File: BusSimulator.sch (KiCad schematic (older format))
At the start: 100 parts, among them IC1 CS30CL, IC2 CS30CL, IC3 CS30CL, J1 CONN_3-6318491-6, J2 OSTTA024163, J3 Conn_01x03, J4 Conn_01x03, J5 Conn_01x02, J6 Conn_01x03, Q1 MOSFET_N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

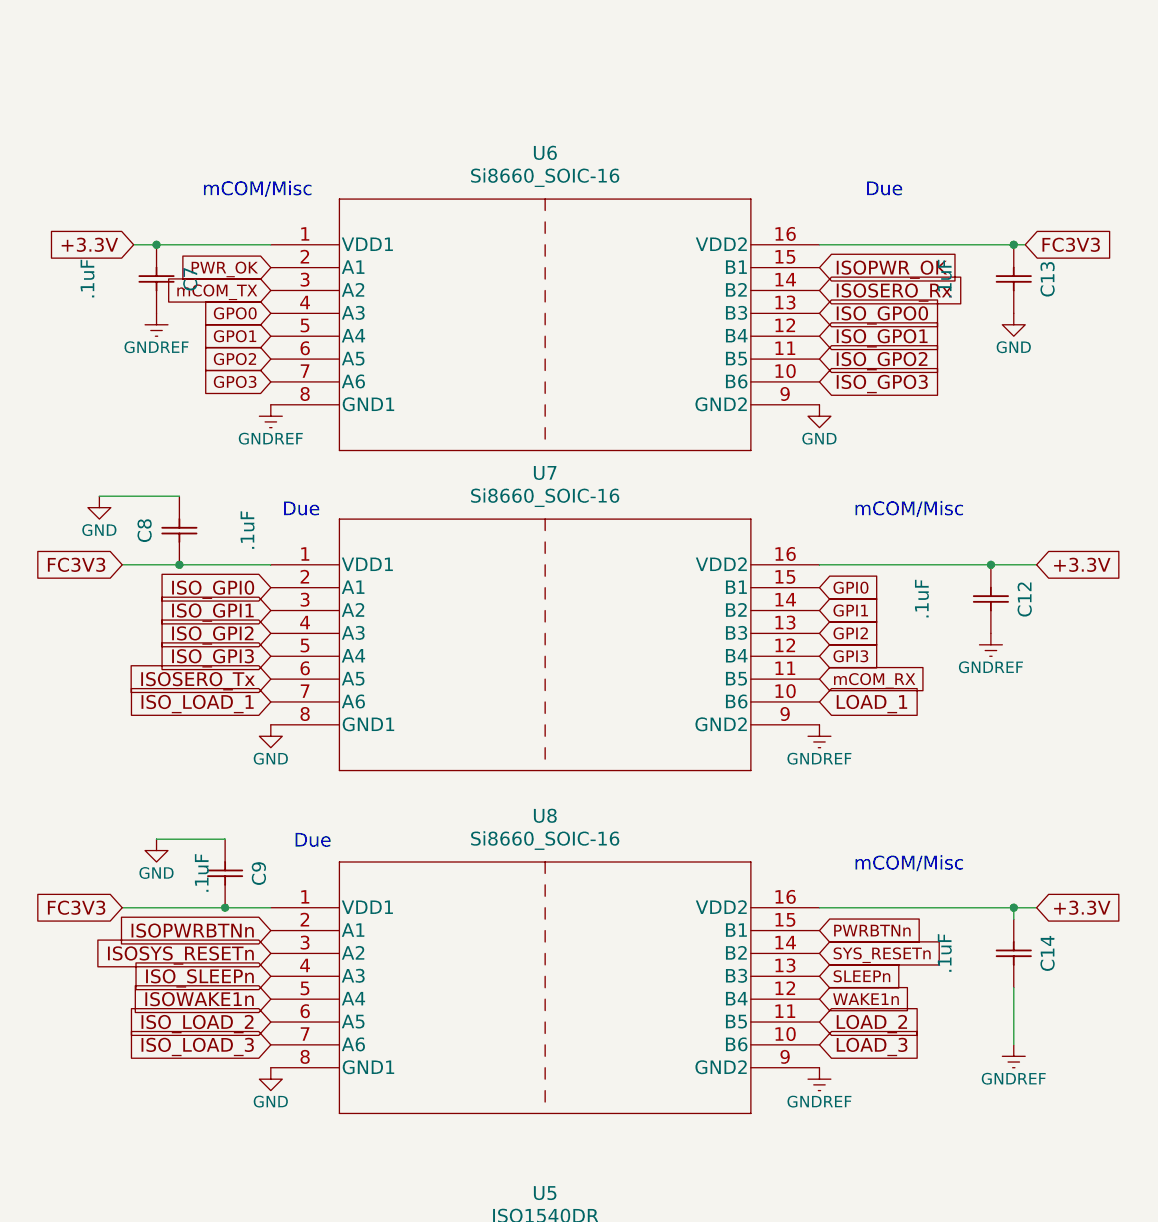
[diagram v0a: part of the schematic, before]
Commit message: Organize isolator nets and arrange PCB components
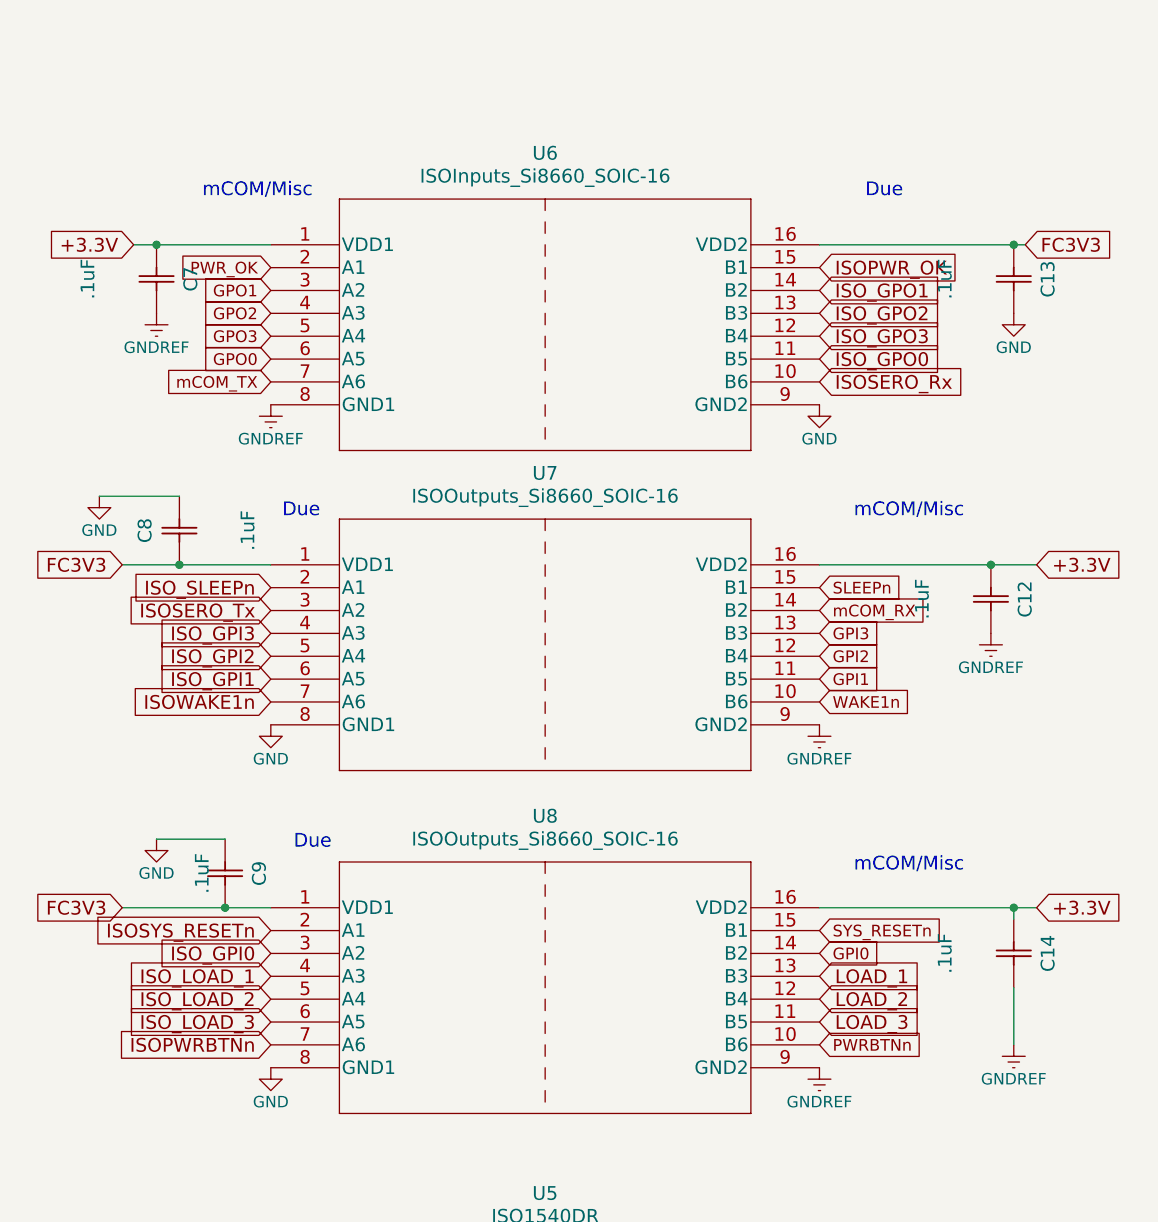
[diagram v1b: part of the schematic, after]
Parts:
- U6: value Si8660_SOIC-16 -> ISOInputs_Si8660_SOIC-16
- U7, U8: value Si8660_SOIC-16 -> ISOOutputs_Si8660_SOIC-16
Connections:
- net GPI0: now also U8.14 (B2); no longer U7.15 (B1)
- net GPI1: now also U7.11 (B5); no longer U7.14 (B2)
- net GPI2: now also U7.12 (B4); no longer U7.13 (B3)
- net GPI3: now also U7.13 (B3); no longer U7.12 (B4)
- net GPO0: now also U6.6 (A5); no longer U6.4 (A3)
- net GPO1: now also U6.3 (A2); no longer U6.5 (A4)
- net GPO2: now also U6.4 (A3); no longer U6.6 (A5)
- net GPO3: now also U6.5 (A4); no longer U6.7 (A6)
- net ISOPWRBTNn: now also U8.7 (A6); no longer U8.2 (A1)
- net ISOSERO_Rx: now also U6.10 (B6); no longer U6.14 (B2)
- net ISOSERO_Tx: now also U7.3 (A2); no longer U7.6 (A5)
- net ISOSYS_RESETn: now also U8.2 (A1); no longer U8.3 (A2)
- net ISOWAKE1n: now also U7.7 (A6); no longer U8.5 (A4)
- net ISO_GPI0: now also U8.3 (A2); no longer U7.2 (A1)
- net ISO_GPI1: now also U7.6 (A5); no longer U7.3 (A2)
- net ISO_GPI2: now also U7.5 (A4); no longer U7.4 (A3)
- net ISO_GPI3: now also U7.4 (A3); no longer U7.5 (A4)
- net ISO_GPO0: now also U6.11 (B5); no longer U6.13 (B3)
- net ISO_GPO1: now also U6.14 (B2); no longer U6.12 (B4)
- net ISO_GPO2: now also U6.13 (B3); no longer U6.11 (B5)
- net ISO_GPO3: now also U6.12 (B4); no longer U6.10 (B6)
- net ISO_LOAD_1: now also U8.4 (A3); no longer U7.7 (A6)
- net ISO_LOAD_2: now also U8.5 (A4); no longer U8.6 (A5)
- net ISO_LOAD_3: now also U8.6 (A5); no longer U8.7 (A6)
- net ISO_SLEEPn: now also U7.2 (A1); no longer U8.4 (A3)
- net LOAD_1: now also U8.13 (B3); no longer U7.10 (B6)
- net LOAD_2: now also U8.12 (B4); no longer U8.11 (B5)
- net LOAD_3: now also U8.11 (B5); no longer U8.10 (B6)
- net PWRBTNn: now also U8.10 (B6); no longer U8.15 (B1)
- net SLEEPn: now also U7.15 (B1); no longer U8.13 (B3)
- net SYS_RESETn: now also U8.15 (B1); no longer U8.14 (B2)
- net WAKE1n: now also U7.10 (B6); no longer U8.12 (B4)
- net mCOM_RX: now also U7.14 (B2); no longer U7.11 (B5)
- net mCOM_TX: now also U6.7 (A6); no longer U6.3 (A2)
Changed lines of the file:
@@
 P 1450 9850
 F 0 "U6" H 2650 10250 60  0000 C CNN
-F 1 "Si8660_SOIC-16" H 2650 10150 60  0000 C CNN
+F 1 "ISOInputs_Si8660_SOIC-16" H 2650 10150 60  0000 C CNN
 F 2 "BusSimulator:SI8660BA-B-IS1" H 2650 10090 60  0001 C CNN
 F 3 "" H 1450 9850 60  0000 C CNN
@@
 	1    0    0    -1
 $EndComp
-Text GLabel 3850 13150 2    51   Input ~ 0
+Text GLabel 3850 11850 2    51   Input ~ 0
 WAKE1n
 Text GLabel 1450 9950 0    51   Input ~ 0
 PWR_OK
-Text GLabel 3850 12950 2    51   Input ~ 0
+Text GLabel 3850 12850 2    51   Input ~ 0
 SYS_RESETn
-Text GLabel 3850 12850 2    51   Input ~ 0
+Text GLabel 3850 13350 2    51   Input ~ 0
 PWRBTNn
 Text GLabel 850  9850 0    60   Input ~ 0
@@
 	1    0    0    -1
 $EndComp
-Text GLabel 1450 13150 0    60   Input ~ 0
+Text GLabel 1450 11850 0    60   Input ~ 0
 ISOWAKE1n
 Text GLabel 3850 9950 2    60   Input ~ 0
 ISOPWR_OK
-Text GLabel 1450 12950 0    60   Input ~ 0
+Text GLabel 1450 12850 0    60   Input ~ 0
 ISOSYS_RESETn
-Text GLabel 1450 12850 0    60   Input ~ 0
+Text GLabel 1450 13350 0    60   Input ~ 0
 ISOPWRBTNn
-Text GLabel 3850 11350 2    51   Input ~ 0
+Text GLabel 3850 12950 2    51   Input ~ 0
 GPI0
-Text GLabel 3850 11450 2    51   Input ~ 0
+Text GLabel 3850 11750 2    51   Input ~ 0
 GPI1
+Text GLabel 3850 11650 2    51   Input ~ 0
+GPI2
 Text GLabel 3850 11550 2    51   Input ~ 0
-GPI2
-Text GLabel 3850 11650 2    51   Input ~ 0
 GPI3
+Text GLabel 1450 10050 0    51   Input ~ 0
+GPO1
+Text GLabel 1450 10150 0    51   Input ~ 0
+GPO2
 Text GLabel 1450 10250 0    51   Input ~ 0
-GPO1
+GPO3
 Text GLabel 1450 10350 0    51   Input ~ 0
-GPO2
-Text GLabel 1450 10450 0    51   Input ~ 0
-GPO3
-Text GLabel 1450 10150 0    51   Input ~ 0
 GPO0
 $Comp
@@
 P 1450 11250
 F 0 "U7" H 2650 11650 60  0000 C CNN
-F 1 "Si8660_SOIC-16" H 2650 11550 60  0000 C CNN
+F 1 "ISOOutputs_Si8660_SOIC-16" H 2650 11550 60  0000 C CNN
 F 2 "BusSimulator:SI8660BA-B-IS1" H 2650 11490 60  0001 C CNN
 F 3 "" H 1450 11250 60  0000 C CNN
@@
 P 1450 12750
 F 0 "U8" H 2650 13150 60  0000 C CNN
-F 1 "Si8660_SOIC-16" H 2650 13050 60  0000 C CNN
+F 1 "ISOOutputs_Si8660_SOIC-16" H 2650 13050 60  0000 C CNN
 F 2 "BusSimulator:SI8660BA-B-IS1" H 2650 12990 60  0001 C CNN
 F 3 "" H 1450 12750 60  0000 C CNN
@@
 	1    0    0    -1
 $EndComp
-Text GLabel 3850 11850 2    60   Input ~ 0
+Text GLabel 3850 13050 2    60   Input ~ 0
 LOAD_1
+Text GLabel 3850 13150 2    60   Input ~ 0
+LOAD_2
 Text GLabel 3850 13250 2    60   Input ~ 0
-LOAD_2
-Text GLabel 3850 13350 2    60   Input ~ 0
 LOAD_3
-Text GLabel 3850 13050 2    51   Input ~ 0
+Text GLabel 3850 11350 2    51   Input ~ 0
 SLEEPn
-Text GLabel 1450 13050 0    60   Input ~ 0
+Text GLabel 1450 11350 0    60   Input ~ 0
 ISO_SLEEPn
 $Comp
@@
 Text GLabel 16400 6900 0    60   Input ~ 0
 DUE_SCL
-Text GLabel 1450 11350 0    60   Input ~ 0
+Text GLabel 1450 12950 0    60   Input ~ 0
 ISO_GPI0
-Text GLabel 1450 11450 0    60   Input ~ 0
+Text GLabel 1450 11750 0    60   Input ~ 0
 ISO_GPI1
+Text GLabel 1450 11650 0    60   Input ~ 0
+ISO_GPI2
 Text GLabel 1450 11550 0    60   Input ~ 0
-ISO_GPI2
-Text GLabel 1450 11650 0    60   Input ~ 0
 ISO_GPI3
+Text GLabel 3850 10350 2    60   Input ~ 0
+ISO_GPO0
+Text GLabel 3850 10050 2    60   Input ~ 0
+ISO_GPO1
 Text GLabel 3850 10150 2    60   Input ~ 0
-ISO_GPO0
+ISO_GPO2
 Text GLabel 3850 10250 2    60   Input ~ 0
-ISO_GPO1
-Text GLabel 3850 10350 2    60   Input ~ 0
-ISO_GPO2
-Text GLabel 3850 10450 2    60   Input ~ 0
 ISO_GPO3
-Text GLabel 1450 11850 0    60   Input ~ 0
+Text GLabel 1450 13050 0    60   Input ~ 0
 ISO_LOAD_1
+Text GLabel 1450 13150 0    60   Input ~ 0
+ISO_LOAD_2
 Text GLabel 1450 13250 0    60   Input ~ 0
-ISO_LOAD_2
-Text GLabel 1450 13350 0    60   Input ~ 0
 ISO_LOAD_3
 Text Notes 6300 950  0    60   ~ 0
@@
 	1    0    0    -1
 $EndComp
-Text GLabel 3850 10050 2    60   Input ~ 0
+Text GLabel 3850 10450 2    60   Input ~ 0
 ISOSERO_Rx
-Text GLabel 1450 11750 0    60   Input ~ 0
+Text GLabel 1450 11450 0    60   Input ~ 0
 ISOSERO_Tx
 Text GLabel 16400 5800 0    60   Input ~ 0
@@
 Text Notes 4000 12600 0    60   ~ 0
 mCOM/Misc
-Text GLabel 1450 10050 0    51   Input ~ 0
+Text GLabel 1450 10450 0    51   Input ~ 0
 mCOM_TX
-Text GLabel 3850 11750 2    51   Input ~ 0
+Text GLabel 3850 11450 2    51   Input ~ 0
 mCOM_RX
 Text Notes 1150 9650 0    60   ~ 0

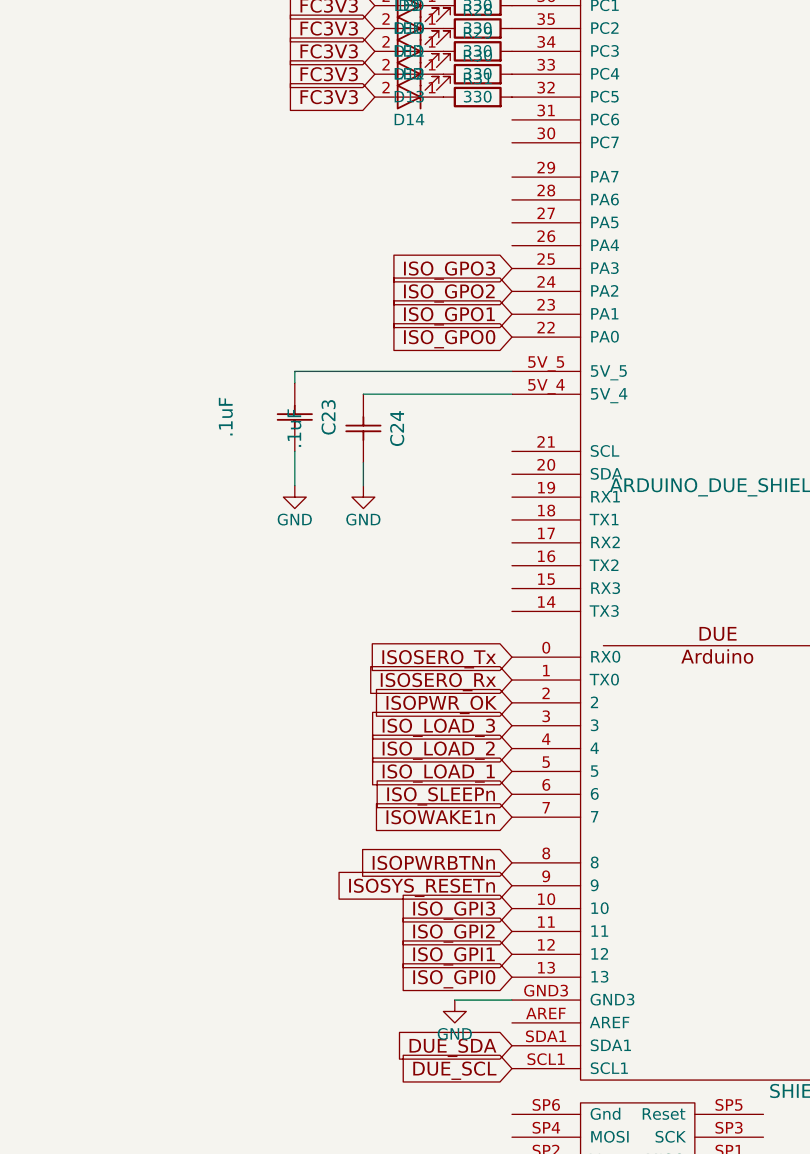
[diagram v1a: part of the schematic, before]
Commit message: Organize Due-to-isolator connection
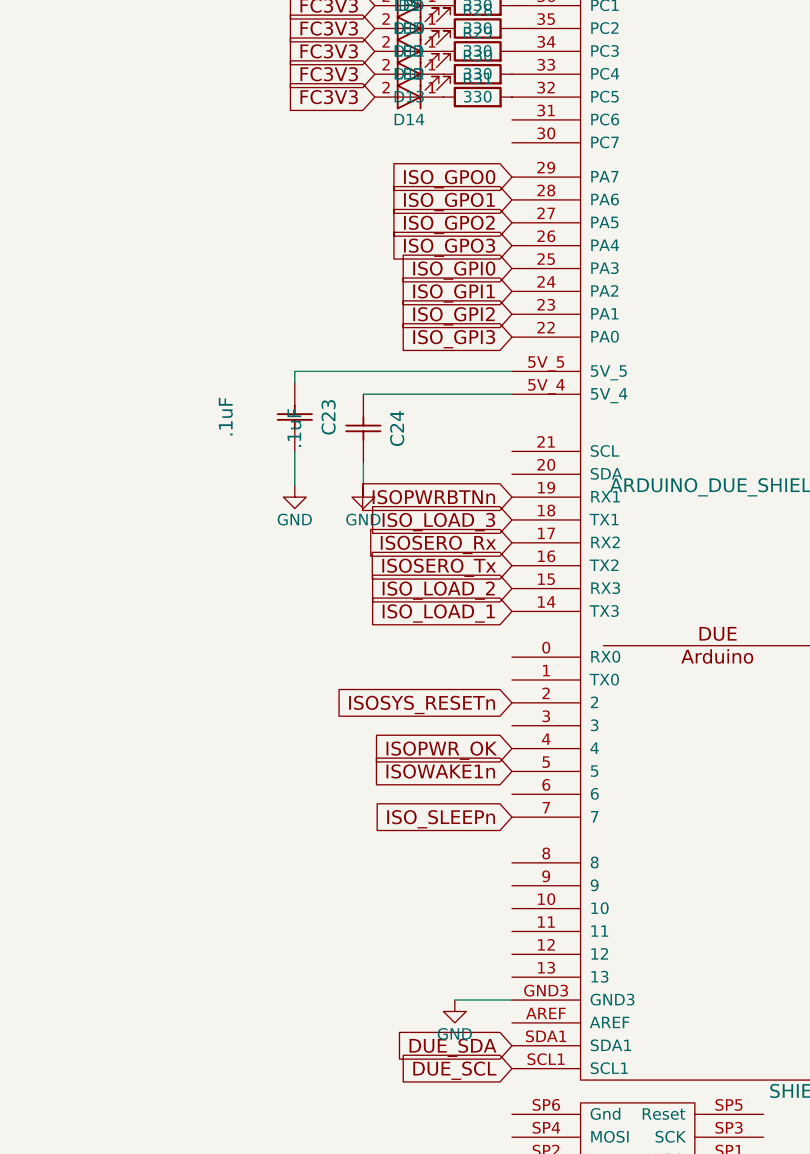
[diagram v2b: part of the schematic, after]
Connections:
- net ISOPWRBTNn: now also SHIELD1.19 (RX1); no longer SHIELD1.8
- net ISOPWR_OK: now also SHIELD1.4; no longer SHIELD1.2
- net ISOSERO_Rx: now also SHIELD1.17 (RX2); no longer SHIELD1.1 (TX0)
- net ISOSERO_Tx: now also SHIELD1.16 (TX2); no longer SHIELD1.0 (RX0)
- net ISOSYS_RESETn: now also SHIELD1.2; no longer SHIELD1.9
- net ISOWAKE1n: now also SHIELD1.5; no longer SHIELD1.7
- net ISO_GPI0: now also SHIELD1.25 (PA3); no longer SHIELD1.13
- net ISO_GPI1: now also SHIELD1.24 (PA2); no longer SHIELD1.12
- net ISO_GPI2: now also SHIELD1.23 (PA1); no longer SHIELD1.11
- net ISO_GPI3: now also SHIELD1.22 (PA0); no longer SHIELD1.10
- net ISO_GPO0: now also SHIELD1.29 (PA7); no longer SHIELD1.22 (PA0)
- net ISO_GPO1: now also SHIELD1.28 (PA6); no longer SHIELD1.23 (PA1)
- net ISO_GPO2: now also SHIELD1.27 (PA5); no longer SHIELD1.24 (PA2)
- net ISO_GPO3: now also SHIELD1.26 (PA4); no longer SHIELD1.25 (PA3)
- net ISO_LOAD_1: now also SHIELD1.14 (TX3); no longer SHIELD1.5
- net ISO_LOAD_2: now also SHIELD1.15 (RX3); no longer SHIELD1.4
- net ISO_LOAD_3: now also SHIELD1.18 (TX1); no longer SHIELD1.3
- net ISO_SLEEPn: now also SHIELD1.7; no longer SHIELD1.6
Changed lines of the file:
@@
 Text GLabel 1450 11450 0    60   Input ~ 0
 ISOSERO_Tx
+Text GLabel 16400 5600 0    60   Input ~ 0
+ISOWAKE1n
+Text GLabel 16400 5300 0    60   Input ~ 0
+ISOSYS_RESETn
+Text GLabel 16400 4400 0    60   Input ~ 0
+ISOPWRBTNn
 Text GLabel 16400 5800 0    60   Input ~ 0
-ISOWAKE1n
-Text GLabel 16400 6100 0    60   Input ~ 0
-ISOSYS_RESETn
-Text GLabel 16400 6000 0    60   Input ~ 0
-ISOPWRBTNn
-Text GLabel 16400 5700 0    60   Input ~ 0
 ISO_SLEEPn
-Text GLabel 16400 6500 0    60   Input ~ 0
+Text GLabel 16400 3400 0    60   Input ~ 0
 ISO_GPI0
-Text GLabel 16400 6400 0    60   Input ~ 0
+Text GLabel 16400 3500 0    60   Input ~ 0
 ISO_GPI1
-Text GLabel 16400 6300 0    60   Input ~ 0
+Text GLabel 16400 3600 0    60   Input ~ 0
 ISO_GPI2
-Text GLabel 16400 6200 0    60   Input ~ 0
+Text GLabel 16400 3700 0    60   Input ~ 0
 ISO_GPI3
-Text GLabel 16400 5600 0    60   Input ~ 0
+Text GLabel 16400 4900 0    60   Input ~ 0
 ISO_LOAD_1
-Text GLabel 16400 5200 0    60   Input ~ 0
+Text GLabel 16400 4600 0    60   Input ~ 0
 ISOSERO_Rx
-Text GLabel 16400 5100 0    60   Input ~ 0
+Text GLabel 16400 4700 0    60   Input ~ 0
 ISOSERO_Tx
-Text GLabel 16400 5300 0    60   Input ~ 0
+Text GLabel 16400 5500 0    60   Input ~ 0
 ISOPWR_OK
-Text GLabel 16400 3700 0    60   Input ~ 0
+Text GLabel 16400 3000 0    60   Input ~ 0
 ISO_GPO0
-Text GLabel 16400 3600 0    60   Input ~ 0
+Text GLabel 16400 3100 0    60   Input ~ 0
 ISO_GPO1
-Text GLabel 16400 3500 0    60   Input ~ 0
+Text GLabel 16400 3200 0    60   Input ~ 0
 ISO_GPO2
-Text GLabel 16400 3400 0    60   Input ~ 0
+Text GLabel 16400 3300 0    60   Input ~ 0
 ISO_GPO3
-Text GLabel 16400 5500 0    60   Input ~ 0
+Text GLabel 16400 4800 0    60   Input ~ 0
 ISO_LOAD_2
-Text GLabel 16400 5400 0    60   Input ~ 0
+Text GLabel 16400 4500 0    60   Input ~ 0
 ISO_LOAD_3
 Text Notes 9400 3650 0    118  ~ 0
